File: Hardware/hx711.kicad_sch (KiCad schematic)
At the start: 3 parts, among them J13 Conn_01x04_Socket, J14 Load Cell 1Kg, U3 HX711

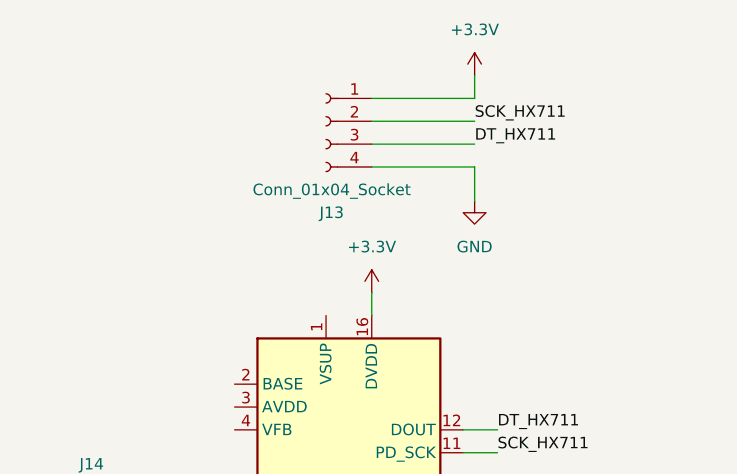
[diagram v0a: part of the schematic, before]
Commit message: class diagrams and hardware diagrams
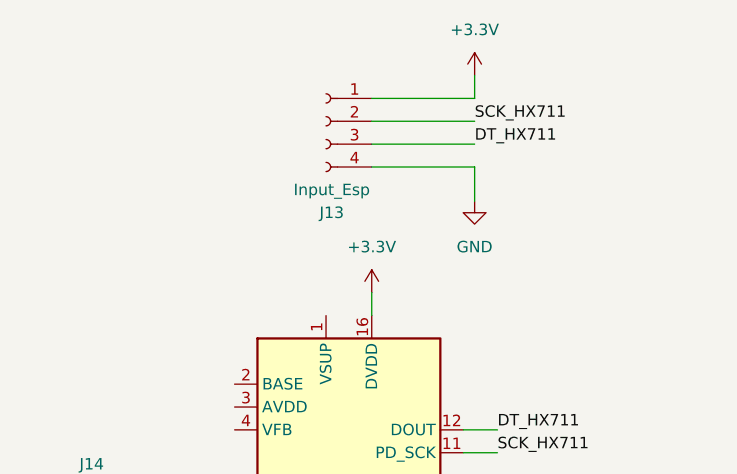
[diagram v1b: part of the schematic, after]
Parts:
- J13: value Conn_01x04_Socket -> Input_Esp
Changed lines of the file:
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@@
       (effects (font (size 1.27 1.27)))
     )
-    (property "Value" "Conn_01x04_Socket" (at 52.705 40.64 0)
+    (property "Value" "Input_Esp" (at 52.705 40.64 0)
       (effects (font (size 1.27 1.27)))
     )
